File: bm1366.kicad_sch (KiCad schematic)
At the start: 46 parts, among them U1 25MHz, U14 BM1366_mode1, U2 SN74AVC4T774PWR

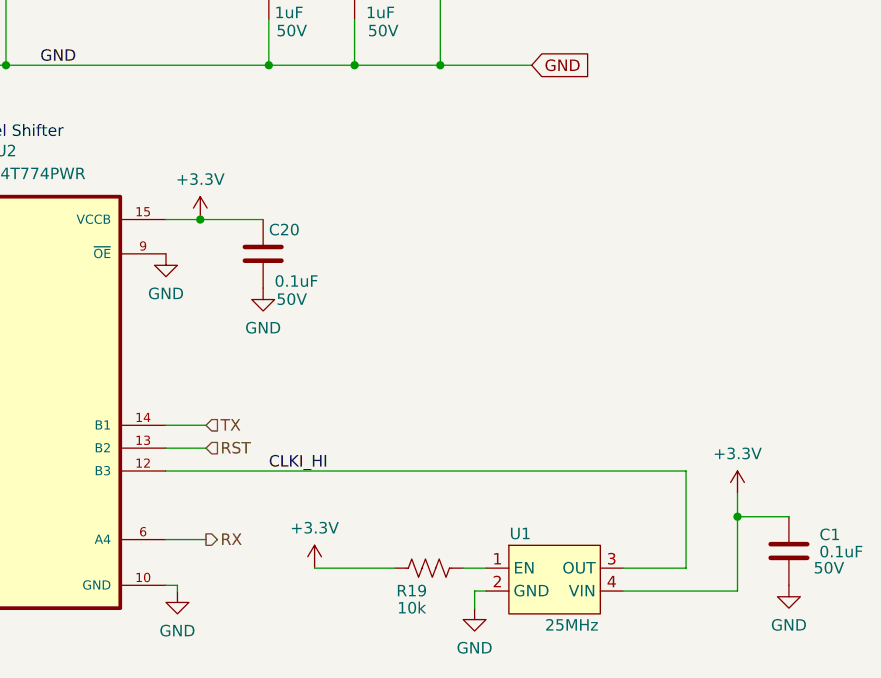
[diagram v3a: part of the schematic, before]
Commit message: 3.3V net fix, PCB progress
Fixed accidental use of both 3V3 and 3.3V to just use 3V3. Worked on PCB
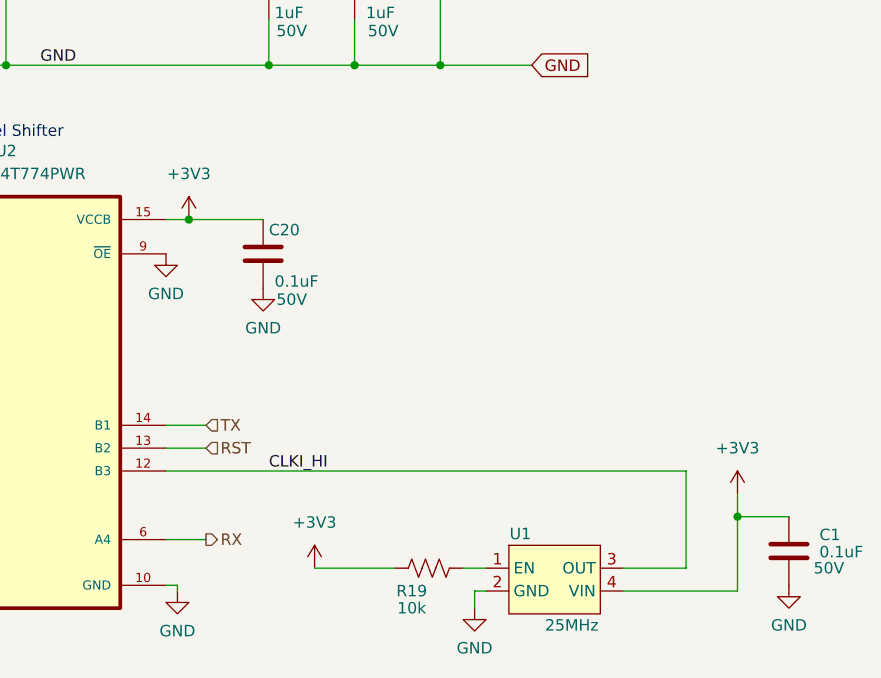
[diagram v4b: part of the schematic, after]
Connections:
- net +3.3V renamed +3V3
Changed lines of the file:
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@@
     (rev "205pd")
   )
+  (junction (at 158.115 123.19) (diameter 0) (color 0 0 0 0)
+  )
   (junction (at 145.415 17.78) (diameter 0) (color 0 0 0 0)
   )
@@
   (junction (at 120.015 135.89) (diameter 0) (color 0 0 0 0)
   )
-  (junction (at 159.385 123.19) (diameter 0) (color 0 0 0 0)
-  )
   (junction (at 134.62 45.085) (diameter 0) (color 0 0 0 0)
   )
@@
   )
   (wire (pts (xy 93.98 106.045) (xy 98.425 106.045))
+    (stroke (width 0) (type default))
+  )
+  (wire (pts (xy 158.115 123.19) (xy 166.37 123.19))
     (stroke (width 0) (type default))
   )
@@
     (stroke (width 0) (type default))
   )
-  (wire (pts (xy 159.385 123.19) (xy 166.37 123.19))
+  (wire (pts (xy 155.575 123.19) (xy 158.115 123.19))
     (stroke (width 0) (type default))
   )
@@
   )
   (wire (pts (xy 155.575 74.295) (xy 168.275 74.295))
-    (stroke (width 0) (type default))
-  )
-  (wire (pts (xy 155.575 123.19) (xy 159.385 123.19))
     (stroke (width 0) (type default))
   )
@@
     )
   )
+  (symbol (lib_id "power:+3V3") (at 219.075 153.67 0) (unit 1)
+    (in_bom yes) (on_board yes) (dnp no) (fields_autoplaced)
+    (property "Reference" "#PWR043" (at 219.075 157.48 0)
+      (effects (font (size 1.27 1.27)) hide)
+    )
+    (property "Value" "+3V3" (at 219.075 148.59 0)
+      (effects (font (size 1.27 1.27)))
+    )
+    (property "Footprint" "" (at 219.075 153.67 0)
+      (effects (font (size 1.27 1.27)) hide)
+    )
+    (property "Datasheet" "" (at 219.075 153.67 0)
+      (effects (font (size 1.27 1.27)) hide)
+    )
+    (pin "1")
+    (instances
+      (project "bitaxeUltra"
+        (path "/e63e39d7-6ac0-4ffd-8aa3-1841a4541b55/4cf9c075-d009-4c35-9949-adda70ae20c7"
+          (reference "#PWR043") (unit 1)
+        )
+      )
+    )
+  )
   (symbol (lib_id "power:+1V2") (at 103.505 91.44 0) (unit 1)
     (in_bom yes) (on_board yes) (dnp no) (fields_autoplaced)
@@
     )
   )
+  (symbol (lib_id "power:+3V3") (at 172.085 161.925 0) (unit 1)
+    (in_bom yes) (on_board yes) (dnp no) (fields_autoplaced)
+    (property "Reference" "#PWR04" (at 172.085 165.735 0)
+      (effects (font (size 1.27 1.27)) hide)
+    )
+    (property "Value" "+3V3" (at 172.085 156.845 0)
+      (effects (font (size 1.27 1.27)))
+    )
+    (property "Footprint" "" (at 172.085 161.925 0)
+      (effects (font (size 1.27 1.27)) hide)
+    )
+    (property "Datasheet" "" (at 172.085 161.925 0)
+      (effects (font (size 1.27 1.27)) hide)
+    )
+    (pin "1")
+    (instances
+      (project "bitaxeUltra"
+        (path "/e63e39d7-6ac0-4ffd-8aa3-1841a4541b55/4cf9c075-d009-4c35-9949-adda70ae20c7"
+          (reference "#PWR04") (unit 1)
+        )
+      )
+    )
+  )
   (symbol (lib_id "Device:C") (at 198.12 45.085 90) (unit 1)
     (in_bom yes) (on_board yes) (dnp no)
@@
         (path "/e63e39d7-6ac0-4ffd-8aa3-1841a4541b55/4cf9c075-d009-4c35-9949-adda70ae20c7"
           (reference "C17") (unit 1)
-        )
-      )
-    )
-  )
-  (symbol (lib_id "power:+3.3V") (at 172.085 161.925 0) (unit 1)
-    (in_bom yes) (on_board yes) (dnp no) (fields_autoplaced)
-    (property "Reference" "#PWR04" (at 172.085 165.735 0)
-      (effects (font (size 1.27 1.27)) hide)
-    )
-    (property "Value" "+3.3V" (at 172.085 157.48 0)
-      (effects (font (size 1.27 1.27)))
-    )
-    (property "Footprint" "" (at 172.085 161.925 0)
-      (effects (font (size 1.27 1.27)) hide)
-    )
-    (property "Datasheet" "" (at 172.085 161.925 0)
-      (effects (font (size 1.27 1.27)) hide)
-    )
-    (pin "1")
-    (instances
-      (project "bitaxeUltra"
-        (path "/e63e39d7-6ac0-4ffd-8aa3-1841a4541b55/4cf9c075-d009-4c35-9949-adda70ae20c7"
-          (reference "#PWR04") (unit 1)
         )
       )
@@
     )
   )
-  (symbol (lib_id "power:+3.3V") (at 159.385 123.19 0) (unit 1)
-    (in_bom yes) (on_board yes) (dnp no) (fields_autoplaced)
-    (property "Reference" "#PWR068" (at 159.385 127 0)
-      (effects (font (size 1.27 1.27)) hide)
-    )
-    (property "Value" "+3.3V" (at 159.385 118.745 0)
-      (effects (font (size 1.27 1.27)))
-    )
-    (property "Footprint" "" (at 159.385 123.19 0)
-      (effects (font (size 1.27 1.27)) hide)
-    )
-    (property "Datasheet" "" (at 159.385 123.19 0)
-      (effects (font (size 1.27 1.27)) hide)
-    )
-    (pin "1")
-    (instances
-      (project "bitaxeUltra"
-        (path "/e63e39d7-6ac0-4ffd-8aa3-1841a4541b55/4cf9c075-d009-4c35-9949-adda70ae20c7"
-          (reference "#PWR068") (unit 1)
-        )
-      )
-    )
-  )
   (symbol (lib_id "power:GND") (at 156.845 164.465 0) (mirror y) (unit 1)
     (in_bom yes) (on_board yes) (dnp no) (fields_autoplaced)
@@
     )
   )
+  (symbol (lib_id "power:+3V3") (at 158.115 123.19 0) (unit 1)
+    (in_bom yes) (on_board yes) (dnp no) (fields_autoplaced)
+    (property "Reference" "#PWR068" (at 158.115 127 0)
+      (effects (font (size 1.27 1.27)) hide)
+    )
+    (property "Value" "+3V3" (at 158.115 118.11 0)
+      (effects (font (size 1.27 1.27)))
+    )
+    (property "Footprint" "" (at 158.115 123.19 0)
+      (effects (font (size 1.27 1.27)) hide)
+    )
+    (property "Datasheet" "" (at 158.115 123.19 0)
+      (effects (font (size 1.27 1.27)) hide)
+    )
+    (pin "1")
+    (instances
+      (project "bitaxeUltra"
+        (path "/e63e39d7-6ac0-4ffd-8aa3-1841a4541b55/4cf9c075-d009-4c35-9949-adda70ae20c7"
+          (reference "#PWR068") (unit 1)
+        )
+      )
+    )
+  )
   (symbol (lib_id "Device:C") (at 176.53 97.155 0) (unit 1)
     (in_bom yes) (on_board yes) (dnp no)
@@
         )
       )
-    )
-  )
-  (symbol (lib_id "power:+3.3V") (at 219.075 153.67 0) (unit 1)
-    (in_bom yes) (on_board yes) (dnp no) (fields_autoplaced)
-    (property "Reference" "#PWR043" (at 219.075 157.48 0)
-      (effects (font (size 1.27 1.27)) hide)
-    )
-    (property "Value" "+3.3V" (at 219.075 149.225 0)
-      (effects (font (size 1.27 1.27)))
-    )
-    (property "Footprint" "" (at 219.075 153.67 0)
-      (effects (font (size 1.27 1.27)) hide)
-    )
-    (property "Datasheet" "" (at 219.075 153.67 0)
-      (effects (font (size 1.27 1.27)) hide)
-    )
-    (pin "1")
-    (instances
-      (project "bitaxeUltra"
-        (path "/e63e39d7-6ac0-4ffd-8aa3-1841a4541b55/4cf9c075-d009-4c35-9949-adda70ae20c7"
-          (reference "#PWR043") (unit 1)
-        )
-      )

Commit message: Layout completed for concept 1
Need to still work on vias and fills, move some parts around.
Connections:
- net +1V2: now also U2.1 (DIR1); no longer U2.8 (DIR4)
- net CI: now also U2.4 (A2); no longer U2.3 (A1)
- net CLKI: now also U2.6 (A4); no longer U2.5 (A3)
- net CLKI_HI: now also U2.11 (B4); no longer U2.12 (B3)
- net GND: now also U2.8 (DIR4); no longer U2.1 (DIR1)
- net RO: now also U2.3 (A1); no longer U2.11 (B4)
- net RST: now also U2.12 (B3); no longer U2.13 (B2)
- net RST_N: now also U2.5 (A3); no longer U2.4 (A2)
- net RX: now also U2.14 (B1); no longer U2.6 (A4)
- net TX: now also U2.13 (B2); no longer U2.14 (B1)
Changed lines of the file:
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@@
     (rev "205pd")
   )
+  (junction (at 120.015 140.97) (diameter 0) (color 0 0 0 0)
+  )
   (junction (at 158.115 123.19) (diameter 0) (color 0 0 0 0)
   )
@@
   (junction (at 132.08 106.045) (diameter 0) (color 0 0 0 0)
   )
-  (junction (at 113.665 123.19) (diameter 0) (color 0 0 0 0)
-  )
   (junction (at 176.53 106.045) (diameter 0) (color 0 0 0 0)
   )
   (junction (at 116.84 123.19) (diameter 0) (color 0 0 0 0)
   )
-  (junction (at 120.015 135.89) (diameter 0) (color 0 0 0 0)
-  )
   (junction (at 134.62 45.085) (diameter 0) (color 0 0 0 0)
   )
@@
   (junction (at 137.795 45.085) (diameter 0) (color 0 0 0 0)
   )
-  (junction (at 120.015 133.35) (diameter 0) (color 0 0 0 0)
-  )
   (junction (at 125.095 30.48) (diameter 0.9144) (color 0 0 0 0)
   )
@@
   (junction (at 191.77 45.085) (diameter 0) (color 0 0 0 0)
   )
+  (junction (at 120.015 138.43) (diameter 0) (color 0 0 0 0)
+  )
   (wire (pts (xy 170.815 20.32) (xy 170.815 17.78))
     (stroke (width 0) (type default))
@@
   )
   (wire (pts (xy 158.115 123.19) (xy 166.37 123.19))
-    (stroke (width 0) (type default))
-  )
-  (wire (pts (xy 113.665 123.19) (xy 113.665 140.97))
     (stroke (width 0) (type default))
   )
@@
     (stroke (width 0) (type default))
   )
-  (wire (pts (xy 120.015 140.97) (xy 113.665 140.97))
+  (wire (pts (xy 116.84 123.19) (xy 116.84 131.445))
     (stroke (width 0) (type default))
   )
@@
     (stroke (width 0) (type default))
   )
-  (wire (pts (xy 155.575 158.75) (xy 160.02 158.75))
-    (stroke (width 0) (type default))
-  )
   (wire (pts (xy 155.575 81.915) (xy 186.055 81.915))
     (stroke (width 0) (type default))
@@
     (stroke (width 0) (type default))
   )
+  (wire (pts (xy 109.855 140.97) (xy 120.015 140.97))
+    (stroke (width 0) (type default))
+  )
   (wire (pts (xy 107.315 45.085) (xy 109.22 45.085))
     (stroke (width 0) (type default))
@@
     (stroke (width 0) (type default))
   )
+  (wire (pts (xy 120.015 138.43) (xy 120.015 140.97))
+    (stroke (width 0) (type default))
+  )
   (wire (pts (xy 103.505 91.44) (xy 106.68 91.44))
     (stroke (width 0) (type default))
@@
   )
   (wire (pts (xy 72.39 45.085) (xy 76.2 45.085))
+    (stroke (width 0) (type default))
+  )
+  (wire (pts (xy 155.575 151.13) (xy 160.02 151.13))
     (stroke (width 0) (type default))
   )
@@
     (stroke (width 0) (type solid))
   )
-  (wire (pts (xy 113.665 123.19) (xy 116.84 123.19))
+  (wire (pts (xy 106.045 123.19) (xy 116.84 123.19))
     (stroke (width 0) (type default))
   )
@@
     (stroke (width 0) (type default))
   )
-  (wire (pts (xy 155.575 151.13) (xy 213.36 151.13))
-    (stroke (width 0) (type default))
-  )
   (wire (pts (xy 155.575 71.755) (xy 168.275 71.755))
     (stroke (width 0) (type default))
@@
     (stroke (width 0) (type default))
   )
-  (wire (pts (xy 120.015 135.89) (xy 120.015 133.35))
-    (stroke (width 0) (type default))
-  )
   (wire (pts (xy 59.69 71.755) (xy 66.675 71.755))
     (stroke (width 0) (type default))
@@
     (stroke (width 0) (type default))
   )
-  (wire (pts (xy 106.045 123.19) (xy 113.665 123.19))
+  (wire (pts (xy 213.36 151.13) (xy 168.275 151.13))
     (stroke (width 0) (type default))
   )
@@
     (stroke (width 0) (type default))
   )
+  (wire (pts (xy 168.275 151.13) (xy 168.275 158.75))
+    (stroke (width 0) (type default))
+  )
   (wire (pts (xy 81.915 66.675) (xy 120.015 66.675))
     (stroke (width 0) (type default))
@@
     (stroke (width 0) (type default))
   )
+  (wire (pts (xy 155.575 158.75) (xy 168.275 158.75))
+    (stroke (width 0) (type default))
+  )
   (text "IO Level Shifter" (at 130.81 114.3 0)
     (effects (font (size 1.27 1.27)) (justify left bottom))
@@
     (effects (font (size 1.27 1.27)) (justify left bottom))
   )
+  (label "CI" (at 113.665 148.59 0) (fields_autoplaced)
+    (effects (font (size 1.27 1.27)) (justify left bottom))
+  )
   (label "GND" (at 141.605 106.045 0) (fields_autoplaced)
     (effects (font (size 1.27 1.27)) (justify left bottom))
   )
-  (label "CLKI_HI" (at 167.005 151.13 0) (fields_autoplaced)
+  (label "CLKI_HI" (at 168.275 151.13 0) (fields_autoplaced)
     (effects (font (size 1.27 1.27)) (justify left bottom))
   )
@@
     (effects (font (size 1.27 1.27)) (justify right bottom))
   )
+  (label "RO" (at 113.665 146.05 0) (fields_autoplaced)
+    (effects (font (size 1.27 1.27)) (justify left bottom))
+  )
   (label "VDD3_1" (at 212.09 59.055 0) (fields_autoplaced)
     (effects (font (size 1.27 1.27)) (justify left bottom))
@@
     (effects (font (size 1.27 1.27)) (justify right bottom))
   )
-  (label "CI" (at 113.665 146.05 0) (fields_autoplaced)
-    (effects (font (size 1.27 1.27)) (justify left bottom))
-  )
   (label "VDD3_0" (at 111.125 59.055 0) (fields_autoplaced)
     (effects (font (size 1.27 1.27)) (justify left bottom))
@@
     (effects (font (size 1.27 1.27)) (justify left bottom))
   )
-  (label "RO" (at 113.665 158.75 0) (fields_autoplaced)
+  (label "CLKI" (at 113.665 158.75 0) (fields_autoplaced)
+    (effects (font (size 1.27 1.27)) (justify left bottom))
+  )
+  (label "RST_N" (at 113.665 151.13 0) (fields_autoplaced)
     (effects (font (size 1.27 1.27)) (justify left bottom))
   )
@@
   )
   (label "INV_CLKO" (at 212.09 76.835 0) (fields_autoplaced)
-    (effects (font (size 1.27 1.27)) (justify left bottom))
-  )
-  (label "RST_N" (at 113.665 148.59 0) (fields_autoplaced)
-    (effects (font (size 1.27 1.27)) (justify left bottom))
-  )
-  (label "CLKI" (at 113.665 151.13 0) (fields_autoplaced)
     (effects (font (size 1.27 1.27)) (justify left bottom))
   )
@@
     )
   )
-  (hierarchical_label "RST" (shape input) (at 160.02 148.59 0) (fields_autoplaced)
-    (effects (font (size 1.27 1.27)) (justify left))
-  )
-  (hierarchical_label "TX" (shape input) (at 160.02 146.05 0) (fields_autoplaced)
+  (hierarchical_label "RST" (shape input) (at 160.02 151.13 0) (fields_autoplaced)
     (effects (font (size 1.27 1.27)) (justify left))
   )
@@
     (effects (font (size 1.27 1.27)) (justify right))
   )
-  (hierarchical_label "RX" (shape output) (at 160.02 158.75 0) (fields_autoplaced)
+  (hierarchical_label "RX" (shape output) (at 160.02 146.05 0) (fields_autoplaced)
     (effects (font (size 1.27 1.27)) (justify left))
+  )
+  (hierarchical_label "TX" (shape input) (at 160.02 148.59 0) (fields_autoplaced)
+    (effects (font (size 1.27 1.27)) (justify left))
+  )
+  (symbol (lib_id "power:GND") (at 109.855 140.97 0) (mirror y) (unit 1)
+    (in_bom yes) (on_board yes) (dnp no) (fields_autoplaced)
+    (property "Reference" "#PWR045" (at 109.855 147.32 0)
+      (effects (font (size 1.27 1.27)) hide)
+    )
+    (property "Value" "GND" (at 109.855 145.415 0)
+      (effects (font (size 1.27 1.27)))
+    )
+    (property "Footprint" "" (at 109.855 140.97 0)
+      (effects (font (size 1.27 1.27)) hide)
+    )
+    (property "Datasheet" "" (at 109.855 140.97 0)
+      (effects (font (size 1.27 1.27)) hide)
+    )
+    (pin "1")
+    (instances
+      (project "bitaxeUltra"
+        (path "/e63e39d7-6ac0-4ffd-8aa3-1841a4541b55/4cf9c075-d009-4c35-9949-adda70ae20c7"
+          (reference "#PWR045") (unit 1)
+        )
+      )
+    )
   )
   (symbol (lib_id "power:+1V0") (at 97.155 88.265 0) (unit 1)
@@
   )
   (symbol (lib_id "power:+3V3") (at 172.085 161.925 0) (unit 1)
-    (in_bom yes) (on_board yes) (dnp no) (fields_autoplaced)
+    (in_bom yes) (on_board yes) (dnp no)
     (property "Reference" "#PWR04" (at 172.085 165.735 0)
       (effects (font (size 1.27 1.27)) hide)
     )
-    (property "Value" "+3V3" (at 172.085 156.845 0)
+    (property "Value" "+3V3" (at 172.085 158.115 0)
       (effects (font (size 1.27 1.27)))
     )
@@
         )
       )
-    )
-  )
-  (symbol (lib_id "power:GND") (at 116.84 131.445 0) (mirror y) (unit 1)
-    (in_bom yes) (on_board yes) (dnp no) (fields_autoplaced)
-    (property "Reference" "#PWR045" (at 116.84 137.795 0)
-      (effects (font (size 1.27 1.27)) hide)
-    )
-    (property "Value" "GND" (at 116.84 135.89 0)
-      (effects (font (size 1.27 1.27)))
-    )
-    (property "Footprint" "" (at 116.84 131.445 0)
-      (effects (font (size 1.27 1.27)) hide)
-    )
-    (property "Datasheet" "" (at 116.84 131.445 0)
-      (effects (font (size 1.27 1.27)) hide)
-    )
-    (pin "1")
-    (instances
-      (project "bitaxeUltra"
-        (path "/e63e39d7-6ac0-4ffd-8aa3-1841a4541b55/4cf9c075-d009-4c35-9949-adda70ae20c7"
-          (reference "#PWR045") (unit 1)
-        )
-      )
